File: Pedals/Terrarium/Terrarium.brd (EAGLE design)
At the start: 59.4 x 73 mm, 46 parts, among them IC1 TL072CP, IC2 LM78L05, SW5 3PDTTOGGLE

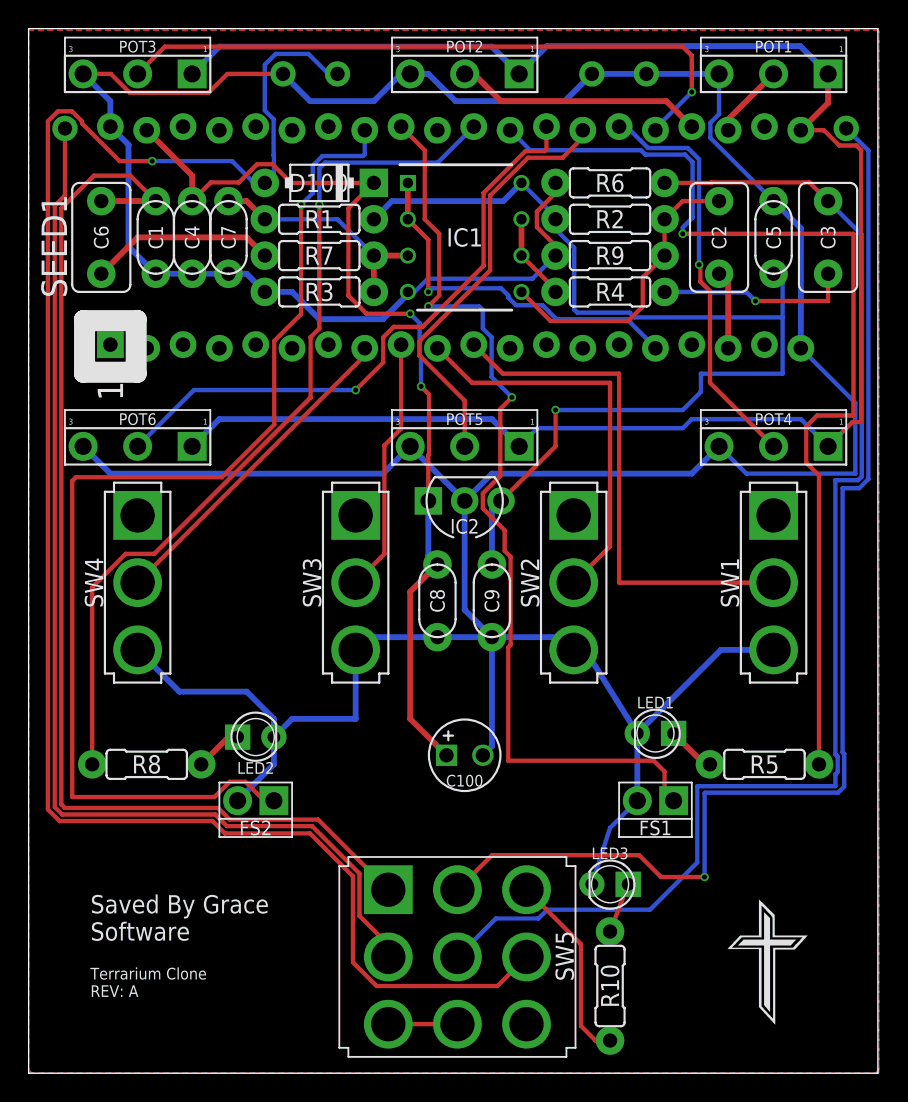
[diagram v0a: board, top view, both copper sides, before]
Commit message: Fix true bypass circuit on Terrarium
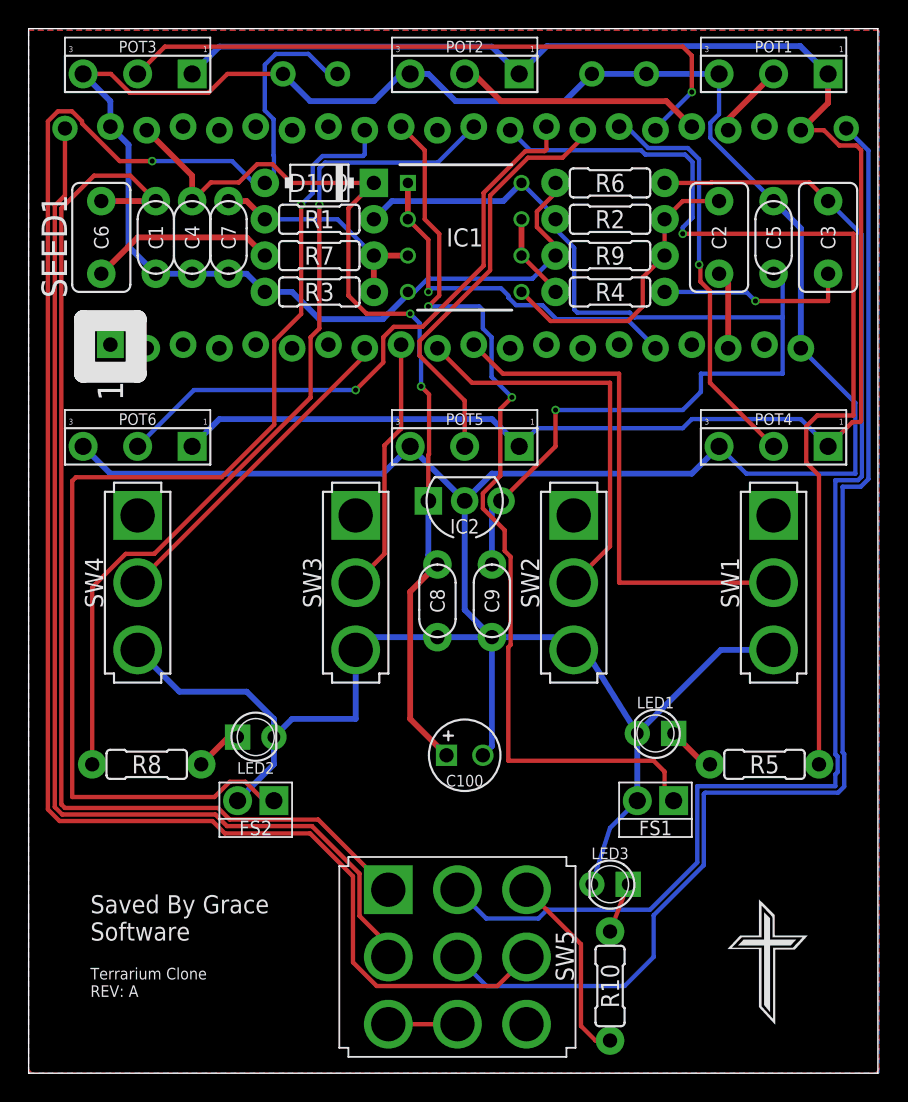
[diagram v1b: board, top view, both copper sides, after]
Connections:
- removed net N$18: OUT.P$1, SW5.B1
- new net N$21: OUT.P$1, SW5.B2
- net N$11: now also SW5.B1; no longer SW5.B2
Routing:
- net N$21: track 0.00 -> 86.4 mm
- net N$18: track 82.8 -> 0.00 mm, vias 1 -> 0
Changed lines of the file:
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@@
 <wire x1="47.71953125" y1="62.2648" x2="54.5752" y2="62.2648" width="0.3048" layer="1"/>
 <wire x1="54.5752" y1="62.2648" x2="55.88" y2="60.96" width="0.3048" layer="1"/>
-<contactref element="SW5" pad="B2"/>
-<wire x1="35.63573125" y1="10.8152" x2="36.25053125" y2="11.43" width="0.3048" layer="16"/>
+<wire x1="36.25053125" y1="11.43" x2="35.63573125" y2="10.8152" width="0.3048" layer="16"/>
 <wire x1="36.25053125" y1="11.43" x2="43.434" y2="11.43" width="0.3048" layer="16"/>
-<wire x1="29.972" y1="8.128" x2="32.6592" y2="10.8152" width="0.3048" layer="16"/>
-<wire x1="32.6592" y1="10.8152" x2="35.63573125" y2="10.8152" width="0.3048" layer="16"/>
 <wire x1="43.434" y1="11.43" x2="46.736" y2="14.732" width="0.3048" layer="16"/>
 <wire x1="46.736" y1="14.732" x2="46.736" y2="20.066" width="0.3048" layer="16"/>
@@
 <wire x1="58.2422" y1="58.5978" x2="55.88" y2="60.96" width="0.3048" layer="16"/>
 <wire x1="58.2422" y1="41.72061875" x2="58.2422" y2="58.5978" width="0.3048" layer="16"/>
+<contactref element="SW5" pad="B1"/>
+<wire x1="31.9848" y1="10.8152" x2="29.972" y2="12.828" width="0.3048" layer="16"/>
+<wire x1="35.63573125" y1="10.8152" x2="31.9848" y2="10.8152" width="0.3048" layer="16"/>
 </signal>
 <signal name="N$12">
@@
 <wire x1="13.055725" y1="18.0848" x2="13.868525" y2="17.272" width="0.3048" layer="1"/>
 </signal>
-<signal name="N$18">
-<contactref element="SW5" pad="B1"/>
-<contactref element="OUT" pad="P$1"/>
-<wire x1="57.15" y1="66.04" x2="58.6994" y2="64.4906" width="0.3048" layer="16"/>
-<wire x1="58.6994" y1="41.5312375" x2="58.0621625" y2="40.894" width="0.3048" layer="16"/>
-<wire x1="58.0621625" y1="40.894" x2="56.896" y2="40.894" width="0.3048" layer="16"/>
-<wire x1="56.57738125" y1="19.6088" x2="47.2948" y2="19.6088" width="0.3048" layer="16"/>
-<wire x1="47.2948" y1="19.6088" x2="47.244" y2="19.558" width="0.3048" layer="16"/>
-<wire x1="56.896" y1="40.894" x2="56.896" y2="22.43085" width="0.3048" layer="16"/>
-<wire x1="56.896" y1="22.43085" x2="57.007" y2="22.31985" width="0.3048" layer="16"/>
-<wire x1="57.007" y1="22.31985" x2="57.007" y2="20.03841875" width="0.3048" layer="16"/>
-<wire x1="57.007" y1="20.03841875" x2="56.57738125" y2="19.6088" width="0.3048" layer="16"/>
-<wire x1="47.244" y1="19.558" x2="47.244" y2="13.716" width="0.3048" layer="16"/>
-<wire x1="58.6994" y1="64.4906" x2="58.6994" y2="41.5312375" width="0.3048" layer="16"/>
-<via x="47.244" y="13.716" extent="1-16" drill="0.35"/>
-<wire x1="47.244" y1="13.716" x2="44.196" y2="13.716" width="0.3048" layer="1"/>
-<wire x1="44.196" y1="13.716" x2="42.672" y2="15.24" width="0.3048" layer="1"/>
-<wire x1="42.672" y1="15.24" x2="32.384" y2="15.24" width="0.3048" layer="1"/>
-<wire x1="32.384" y1="15.24" x2="29.972" y2="12.828" width="0.3048" layer="1"/>
-</signal>
 <signal name="BYPASS">
+<contactref element="SW5" pad="A3"/>
 <contactref element="SW5" pad="B3"/>
-<contactref element="SW5" pad="A3"/>
 <wire x1="25.142" y1="3.428" x2="29.972" y2="3.428" width="0.3048" layer="1"/>
 </signal>
@@
 <wire x1="40.64" y1="9.906" x2="41.91" y2="13.208" width="0.3048" layer="1"/>
 </signal>
+<signal name="N$21">
+<contactref element="OUT" pad="P$1"/>
+<contactref element="SW5" pad="B2"/>
+<wire x1="29.972" y1="8.128" x2="32.004" y2="6.096" width="0.3048" layer="16"/>
+<wire x1="32.004" y1="6.096" x2="41.656" y2="6.096" width="0.3048" layer="16"/>
+<wire x1="41.656" y1="6.096" x2="43.688" y2="8.128" width="0.3048" layer="16"/>
+<wire x1="43.688" y1="11.03741875" x2="47.1932" y2="14.54261875" width="0.3048" layer="16"/>
+<wire x1="47.1932" y1="14.54261875" x2="47.1932" y2="19.5072" width="0.3048" layer="16"/>
+<wire x1="47.2948" y1="19.6088" x2="56.57738125" y2="19.6088" width="0.3048" layer="16"/>
+<wire x1="57.007" y1="22.31985" x2="56.896" y2="22.43085" width="0.3048" layer="16"/>
+<wire x1="56.57738125" y1="19.6088" x2="57.007" y2="20.03841875" width="0.3048" layer="16"/>
+<wire x1="57.007" y1="20.03841875" x2="57.007" y2="22.31985" width="0.3048" layer="16"/>
+<wire x1="56.896" y1="40.9956" x2="58.1637625" y2="40.9956" width="0.3048" layer="16"/>
+<wire x1="58.1637625" y1="40.9956" x2="58.6994" y2="41.5312375" width="0.3048" layer="16"/>
+<wire x1="58.6994" y1="64.4906" x2="57.15" y2="66.04" width="0.3048" layer="16"/>
+<wire x1="43.688" y1="8.128" x2="43.688" y2="11.03741875" width="0.3048" layer="16"/>
+<wire x1="47.1932" y1="19.5072" x2="47.2948" y2="19.6088" width="0.3048" layer="16"/>
+<wire x1="56.896" y1="22.43085" x2="56.896" y2="40.9956" width="0.3048" layer="16"/>
+<wire x1="58.6994" y1="41.5312375" x2="58.6994" y2="64.4906" width="0.3048" layer="16"/>
+</signal>
 </signals>
